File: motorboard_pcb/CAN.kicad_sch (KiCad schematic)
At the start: 19 parts, among them J1 RJ45, J2 RJ45, J3 Conn_01x02_Pin, U2 TCAN1042HGVDQ1

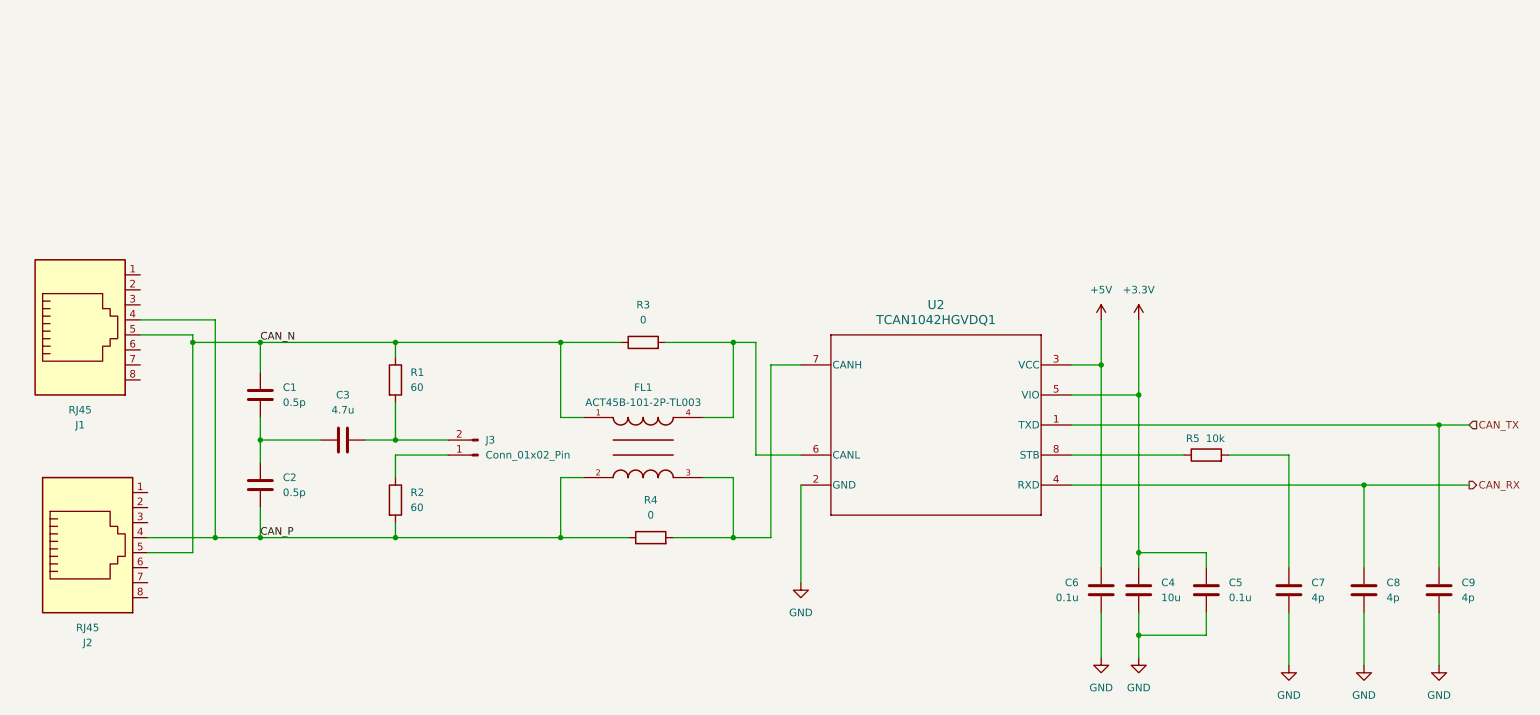
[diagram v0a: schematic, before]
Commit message: switch isolator for SPI, output stage (DAC, op amp)
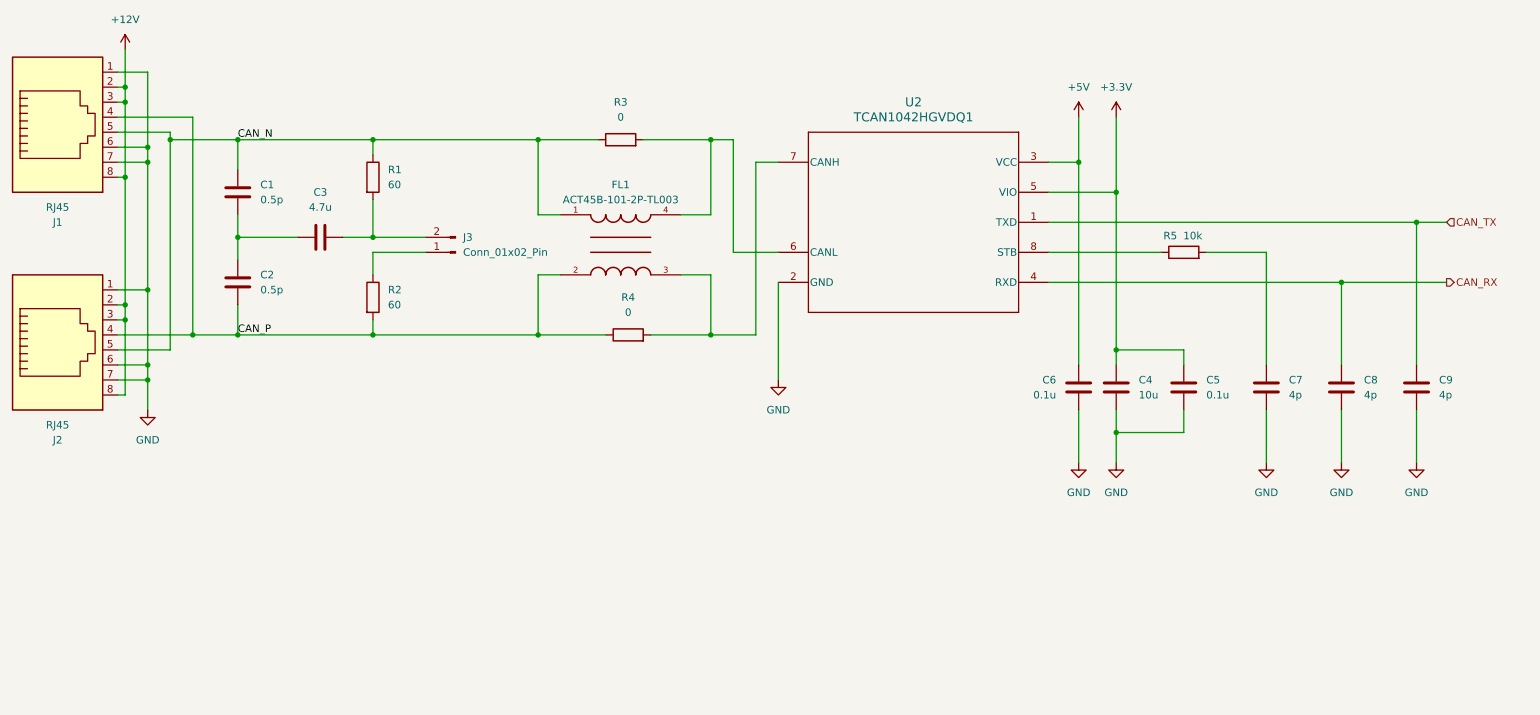
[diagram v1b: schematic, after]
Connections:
- net GND: now also J1.1, J1.6, J1.7, J2.1, J2.6, J2.7
- net +12V: now reaches J2.2
- net +12V: now also J1.2, J1.3, J1.8, J2.3, J2.8
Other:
- moved on the sheet: C1, C2, C3, C4, C5, C6, C7, C8, C9, FL1, J1, J2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

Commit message: Schematic done, pending review
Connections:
- net +12V renamed +12VL
- net +3.3V renamed +3.3VL
- net +5V renamed +5VL
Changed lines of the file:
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@@
 			)
 		)
-		(property "Value" "+12V"
-			(at 41.91 21.59 0)
-			(effects
-				(font
-					(size 1.27 1.27)
-				)
+		(property "Value" "+12VL"
+			(at 44.45 25.3999 0)
+			(effects
+				(font
+					(size 1.27 1.27)
+				)
+				(justify left)
 			)
 		)
@@
 		(on_board yes)
 		(dnp no)
-		(fields_autoplaced yes)
 		(property "Reference" "#PWR02"
 			(at 209.55 41.91 0)
@@
 			)
 		)
-		(property "Value" "+3.3V"
-			(at 209.55 33.02 0)
-			(effects
-				(font
-					(size 1.27 1.27)
-				)
+		(property "Value" "+3.3VL"
+			(at 208.788 33.02 0)
+			(effects
+				(font
+					(size 1.27 1.27)
+				)
+				(justify left)
 			)
 		)
@@
 		(on_board yes)
 		(dnp no)
-		(fields_autoplaced yes)
 		(property "Reference" "#PWR04"
 			(at 203.2 41.91 0)
@@
 			)
 		)
-		(property "Value" "+5V"
-			(at 203.2 33.02 0)
-			(effects
-				(font
-					(size 1.27 1.27)
-				)
-			)
-		)
+		(property "Value" "+5VL"
+			(at 200.66 33.02 0)
+			(effects
+				(font
+					(size 1.27 1.27)
+				)
+				(justify left)
+			)
+		)

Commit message: Initial layout, all resistors/caps are 0602
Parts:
- C1, C2, C3, C4, C5, C6, C7, C8, C9: footprint (none) -> Capacitor_SMD:C_0603_1608Metric
- R1, R2, R3, R4, R5: footprint (none) -> Resistor_SMD:R_0603_1608Metric
- U2: footprint D0008A_N -> TCAN1042:D0008A_L
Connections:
- net GND: now also C1.1, C2.2, C3.2
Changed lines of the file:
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@@
+	(wire
+		(pts
+			(xy 59.69 58.42) (xy 60.96 58.42)
+		)
+		(stroke
+			(width 0)
+			(type default)
+		)
+	)
 	(wire
 		(pts
@@
 			)
 		)
-		(property "Footprint" ""
+		(property "Footprint" "Capacitor_SMD:C_0603_1608Metric"
 			(at 210.5152 87.63 0)
 			(effects
@@
 			)
 		)
-		(property "Footprint" ""
+		(property "Footprint" "Capacitor_SMD:C_0603_1608Metric"
 			(at 248.6152 87.63 0)
 			(effects
@@
 			)
 		)
-		(property "Footprint" ""
+		(property "Footprint" "Capacitor_SMD:C_0603_1608Metric"
 			(at 59.9948 46.99 0)
 			(effects
@@
 			)
 		)
-		(property "Footprint" ""
+		(property "Footprint" "Resistor_SMD:R_0603_1608Metric"
 			(at 82.042 68.58 90)
 			(effects
@@
 			)
 		)
-		(property "Footprint" ""
+		(property "Footprint" "Resistor_SMD:R_0603_1608Metric"
 			(at 220.98 62.738 90)
 			(effects
@@
 			)
 		)
-		(property "Footprint" ""
+		(property "Footprint" "Capacitor_SMD:C_0603_1608Metric"
 			(at 221.9452 87.63 0)
 			(effects
@@
 			)
 		)
-		(property "Footprint" ""
+		(property "Footprint" "Resistor_SMD:R_0603_1608Metric"
 			(at 127 76.708 90)
 			(effects
@@
 			)
 		)
-		(property "Footprint" ""
+		(property "Footprint" "Capacitor_SMD:C_0603_1608Metric"
 			(at 71.12 59.3852 0)
 			(effects
@@
 			)
 		)
-		(property "Footprint" ""
+		(property "Footprint" "Capacitor_SMD:C_0603_1608Metric"
 			(at 204.1652 80.01 0)
 			(effects
@@
 			)
 		)
-		(property "Footprint" "D0008A_N"
+		(property "Footprint" "TCAN1042:D0008A_L"
 			(at 175.26 55.88 0)
 			(effects
@@
 			)
 		)
-		(property "Footprint" ""
+		(property "Footprint" "Resistor_SMD:R_0603_1608Metric"
 			(at 125.73 43.688 90)
 			(effects
@@
 			)
 		)
-		(property "Footprint" ""
+		(property "Footprint" "Capacitor_SMD:C_0603_1608Metric"
 			(at 235.9152 87.63 0)
 			(effects
@@
 			)
 		)
-		(property "Footprint" ""
+		(property "Footprint" "Capacitor_SMD:C_0603_1608Metric"
 			(at 261.3152 87.63 0)
 			(effects
@@
 			)
 		)
-		(property "Footprint" ""
+		(property "Footprint" "Capacitor_SMD:C_0603_1608Metric"
 			(at 59.9948 62.23 0)
 			(effects
@@
 			)
 		)
-		(property "Footprint" ""
+		(property "Footprint" "Resistor_SMD:R_0603_1608Metric"
 			(at 82.042 48.26 90)
 			(effects
@@
 					(unit 1)
 				)
+			)
+		)
+	)
+	(symbol
+		(lib_id "power:GND")
+		(at 59.69 58.42 270)
+		(unit 1)
+		(exclude_from_sim no)
+		(in_bom yes)
+		(on_board yes)
+		(dnp no)
+		(property "Reference" "#PWR042"
+			(at 53.34 58.42 0)
+			(effects
+				(font
+					(size 1.27 1.27)
+				)
+				(hide yes)
+			)
+		)
+		(property "Value" "GND"
+			(at 58.166 60.96 90)
+			(effects
+				(font
+					(size 1.27 1.27)
+				)
+				(justify right)
+			)
+		)
+		(property "Footprint" ""
+			(at 59.69 58.42 0)
+			(effects
+				(font
+					(size 1.27 1.27)
+				)
+				(hide yes)
+			)
+		)
+		(property "Datasheet" ""
+			(at 59.69 58.42 0)
+			(effects
+				(font
+					(size 1.27 1.27)
+				)
+				(hide yes)
+			)
+		)
+		(property "Description" "Power symbol creates a global label with name \"GND\" , ground"
+			(at 59.69 58.42 0)
+			(effects
+				(font
+					(size 1.27 1.27)
+				)
+				(hide yes)
+			)
+		)
+		(pin "1"
+		)
+		(instances
+			(project "motorboard"
+				(path "/fa713205-4357-49d0-ad77-7aa2864b7782/33cf1546-c866-454a-875b-d10285cc82c3"
+					(reference "#PWR042")
+					(unit 1)
+				)

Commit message: layout finished, silkscreen finished, BOM finished
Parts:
- C1, C2: footprint Capacitor_SMD:C_0603_1608Metric -> Capacitor_SMD:C_0402_1005Metric
- C3, C4: footprint Capacitor_SMD:C_0603_1608Metric -> Capacitor_SMD:C_0805_2012Metric
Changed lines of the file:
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@@
 			)
 		)
-		(property "Footprint" "Capacitor_SMD:C_0603_1608Metric"
+		(property "Footprint" "Capacitor_SMD:C_0805_2012Metric"
 			(at 210.5152 87.63 0)
 			(effects
@@
 			)
 		)
-		(property "Footprint" "Capacitor_SMD:C_0603_1608Metric"
+		(property "Footprint" "Capacitor_SMD:C_0402_1005Metric"
 			(at 59.9948 46.99 0)
 			(effects
@@
 			)
 		)
-		(property "Footprint" "Capacitor_SMD:C_0603_1608Metric"
+		(property "Footprint" "Capacitor_SMD:C_0805_2012Metric"
 			(at 71.12 59.3852 0)
 			(effects
@@
 			)
 		)
-		(property "Footprint" "Capacitor_SMD:C_0603_1608Metric"
+		(property "Footprint" "Capacitor_SMD:C_0402_1005Metric"
 			(at 59.9948 62.23 0)
 			(effects
